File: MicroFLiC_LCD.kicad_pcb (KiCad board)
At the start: 2 copper layers, 50 x 50 mm, 21 parts, among them P1 CONN_02X08, Q1 BCX54-16, U1 MCP4728, U2 TLV2371, U3 74AHCT367, U4 74AHCT367

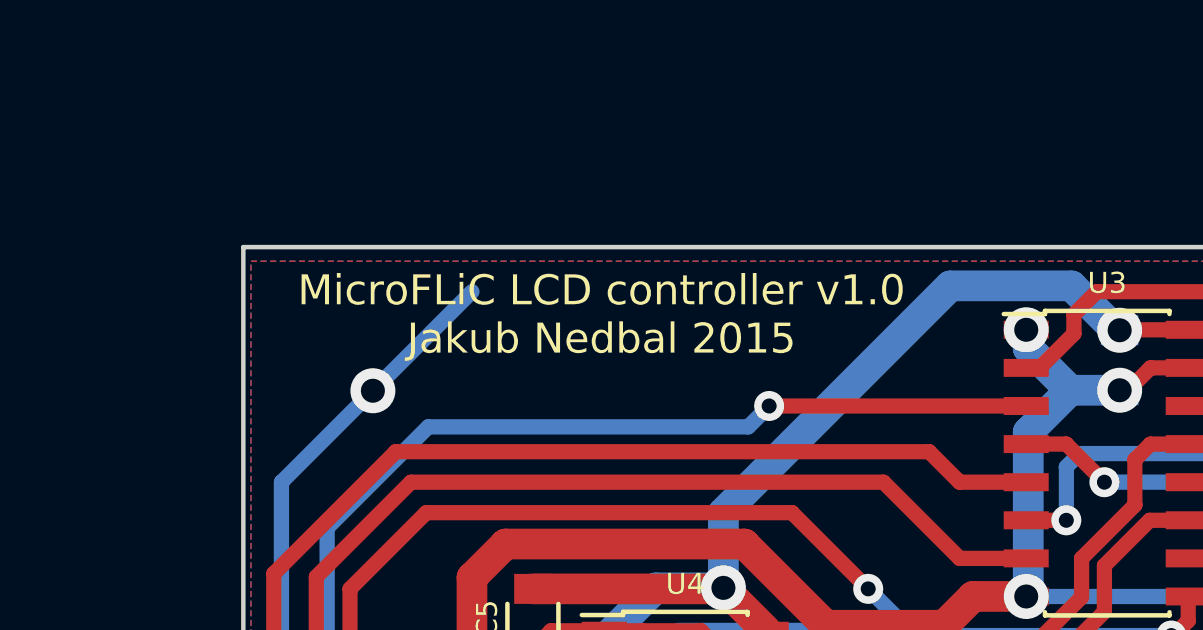
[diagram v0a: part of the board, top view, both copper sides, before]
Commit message: Renamed files, added part description
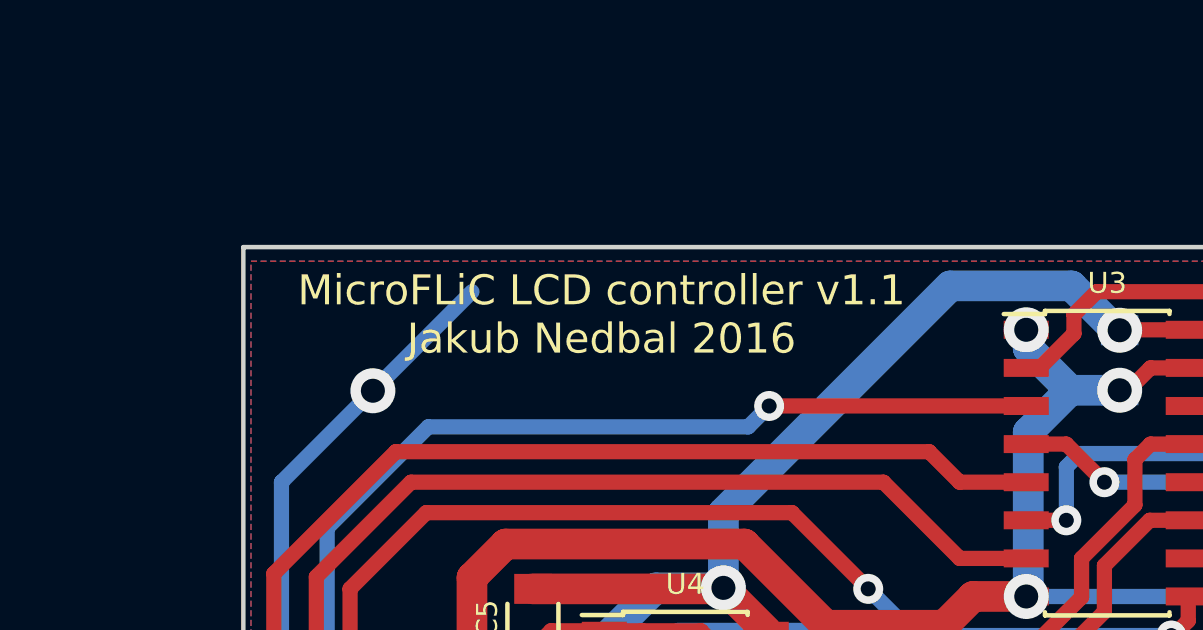
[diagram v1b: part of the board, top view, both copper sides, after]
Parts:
- A1: value Arduino Micro -> Arduino MICRO
- C1: value 10u -> 10u/10V
- C4, C5: value C -> 100n
- P1: value CONN_02X08 -> 2x8 header strip
- R2, R3: value 27R -> 18R(0.5W)
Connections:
- A1 pad 3.3V: (no net) -> Net-(A1-Pad3.3V)
- A1 pad AREF: (no net) -> Net-(A1-PadAREF)
- A1 pad RX: (no net) -> Net-(A1-PadRX)
- A1 pad TX: (no net) -> Net-(A1-PadTX)
- LCD1 pad 10: (no net) -> Net-(LCD1-Pad10)
- LCD1 pad 7: (no net) -> Net-(LCD1-Pad7)
- LCD1 pad 8: (no net) -> Net-(LCD1-Pad8)
- LCD1 pad 9: (no net) -> Net-(LCD1-Pad9)
- U1 pad 5: (no net) -> Net-(U1-Pad5)
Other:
- board text added: "MicroFLiC LCD controller v1.1 Jakub Nedbal 2016"
- board text removed: "MicroFLiC LCD controller v1.0 Jakub Nedbal 2015"
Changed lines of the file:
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@@
-(kicad_pcb (version 4) (host pcbnew 4.0.1-3.201512221402+6198~38~ubuntu14.04.1-stable)
+(kicad_pcb (version 4) (host pcbnew "(2015-12-10 BZR 6367)-product")
   (general
     (links 82)
     (no_connects 0)
-    (area 34.106999 100.104999 132.857001 160.855001)
+    (area 82.220999 110.198999 132.371001 160.349001)
     (thickness 1.6)
     (drawings 72)
@@
     (zones 0)
     (modules 21)
-    (nets 50)
+    (nets 59)
   )
   (page A4)
@@
       (drillshape 0)
       (scaleselection 1)
-      (outputdirectory board/))
+      (outputdirectory board_v1.1/))
   )
   (net 0 "")
@@
   (net 48 /3V3to5V/D4)
   (net 49 "Net-(R4-Pad2)")
+  (net 50 "Net-(A1-PadAREF)")
+  (net 51 "Net-(A1-Pad3.3V)")
+  (net 52 "Net-(A1-PadTX)")
+  (net 53 "Net-(A1-PadRX)")
+  (net 54 "Net-(LCD1-Pad7)")
+  (net 55 "Net-(LCD1-Pad8)")
+  (net 56 "Net-(LCD1-Pad9)")
+  (net 57 "Net-(LCD1-Pad10)")
+  (net 58 "Net-(U1-Pad5)")
   (net_class Default "This is the default net class."
     (clearance 0.2)
@@
     (add_net /~LDAC)
     (add_net GND)
+    (add_net "Net-(A1-Pad3.3V)")
+    (add_net "Net-(A1-PadAREF)")
     (add_net "Net-(A1-PadNC)")
+    (add_net "Net-(A1-PadRX)")
+    (add_net "Net-(A1-PadTX)")
+    (add_net "Net-(LCD1-Pad10)")
+    (add_net "Net-(LCD1-Pad7)")
+    (add_net "Net-(LCD1-Pad8)")
+    (add_net "Net-(LCD1-Pad9)")
     (add_net "Net-(Q1-Pad1)")
     (add_net "Net-(Q1-Pad3)")
@@
     (add_net "Net-(R2-Pad2)")
     (add_net "Net-(R4-Pad2)")
+    (add_net "Net-(U1-Pad5)")
   )
   (module jakub:ArduinoMicro (layer B.Cu)
@@
       (effects (font (size 1.2 1.2) (thickness 0.15)) (justify mirror))
     )
-    (fp_text value "Arduino Micro" (at 26.67 9.634) (layer B.SilkS)
+    (fp_text value "Arduino MICRO" (at 26.67 9.634) (layer B.SilkS)
       (effects (font (size 1.2 1.2) (thickness 0.15)) (justify mirror))
     )
@@
     (pad A0 thru_hole circle (at 36.52 16.62) (size 1.2 1.2) (drill 0.8) (layers *.Cu *.Mask B.SilkS)
       (net 9 /LCD_E))
-    (pad AREF thru_hole circle (at 39.06 16.62) (size 1.2 1.2) (drill 0.8) (layers *.Cu *.Mask B.SilkS))
-    (pad 3.3V thru_hole circle (at 41.6 16.62) (size 1.2 1.2) (drill 0.8) (layers *.Cu *.Mask B.SilkS))
+    (pad AREF thru_hole circle (at 39.06 16.62) (size 1.2 1.2) (drill 0.8) (layers *.Cu *.Mask B.SilkS)
+      (net 50 "Net-(A1-PadAREF)"))
+    (pad 3.3V thru_hole circle (at 41.6 16.62) (size 1.2 1.2) (drill 0.8) (layers *.Cu *.Mask B.SilkS)
+      (net 51 "Net-(A1-Pad3.3V)"))
     (pad 13 thru_hole circle (at 44.14 16.62) (size 1.2 1.2) (drill 0.8) (layers *.Cu *.Mask B.SilkS)
       (net 23 /D13))
@@
     (pad SS thru_hole circle (at 6.04 1.38) (size 1.2 1.2) (drill 0.8) (layers *.Cu *.Mask B.SilkS)
       (net 30 /3V3to5V/D0_5V))
-    (pad TX thru_hole circle (at 8.58 1.38) (size 1.2 1.2) (drill 0.8) (layers *.Cu *.Mask B.SilkS))
-    (pad RX thru_hole circle (at 11.12 1.38) (size 1.2 1.2) (drill 0.8) (layers *.Cu *.Mask B.SilkS))
+    (pad TX thru_hole circle (at 8.58 1.38) (size 1.2 1.2) (drill 0.8) (layers *.Cu *.Mask B.SilkS)
+      (net 52 "Net-(A1-PadTX)"))
+    (pad RX thru_hole circle (at 11.12 1.38) (size 1.2 1.2) (drill 0.8) (layers *.Cu *.Mask B.SilkS)
+      (net 53 "Net-(A1-PadRX)"))
     (pad RST thru_hole circle (at 13.66 1.38) (size 1.2 1.2) (drill 0.8) (layers *.Cu *.Mask B.SilkS)
       (net 25 /3V3to5V/~RST_5V))
@@
       (effects (font (size 0.7 0.7) (thickness 0.11)) (justify mirror))
     )
-    (fp_text value 10u (at 0 -2.1) (layer B.Fab) hide
+    (fp_text value 10u/10V (at 0 -2.1) (layer B.Fab) hide
       (effects (font (size 1 1) (thickness 0.15)) (justify mirror))
     )
@@
       (effects (font (size 0.7 0.7) (thickness 0.11)))
     )
-    (fp_text value 27R (at 0 2.1 180) (layer F.Fab) hide
+    (fp_text value "18R(0.5W)" (at 0 2.1 180) (layer F.Fab) hide
       (effects (font (size 1 1) (thickness 0.15)))
     )
@@
       (effects (font (size 0.7 0.7) (thickness 0.11)))
     )
-    (fp_text value 27R (at 0 2.1 90) (layer F.Fab) hide
+    (fp_text value "18R(0.5W)" (at 0 2.1 90) (layer F.Fab) hide
       (effects (font (size 1 1) (thickness 0.15)))
     )
@@
     (pad 4 smd rect (at -2.2 0.5) (size 1.4 0.3) (layers F.Cu F.Paste F.Mask)
       (net 13 /~LDAC))
-    (pad 5 smd rect (at -2.2 1) (size 1.4 0.3) (layers F.Cu F.Paste F.Mask))
+    (pad 5 smd rect (at -2.2 1) (size 1.4 0.3) (layers F.Cu F.Paste F.Mask)
+      (net 58 "Net-(U1-Pad5)"))
     (pad 6 smd rect (at 2.2 1) (size 1.4 0.3) (layers F.Cu F.Paste F.Mask)
       (net 22 /LCD_BKL_CTRL))
@@
       (effects (font (size 0.7 0.7) (thickness 0.11)) (justify mirror))
     )
-    (fp_text value CONN_02X08 (at 0 3.1 270) (layer B.Fab)
+    (fp_text value "2x8 header strip" (at 0 3.1 270) (layer B.Fab)
       (effects (font (size 1 1) (thickness 0.15)) (justify mirror))
     )
@@
       (effects (font (size 0.7 0.7) (thickness 0.11)) (justify mirror))
     )
-    (fp_text value C (at 0 -2.1 270) (layer B.Fab)
+    (fp_text value 100n (at 0 -2.1 270) (layer B.Fab)
       (effects (font (size 1 1) (thickness 0.15)) (justify mirror))
     )
@@
       (effects (font (size 0.7 0.7) (thickness 0.11)))
     )
-    (fp_text value C (at 0 2.1 360) (layer F.Fab) hide
+    (fp_text value 100n (at 0 2.1 360) (layer F.Fab) hide
       (effects (font (size 1 1) (thickness 0.15)))
     )
@@
     (pad 6 thru_hole circle (at 26.5 27) (size 1.9 1.9) (drill 1) (layers *.Cu *.Mask F.SilkS)
       (net 8 /LCD_D4))
-    (pad 7 thru_hole circle (at 23.96 27) (size 1.9 1.9) (drill 1) (layers *.Cu *.Mask F.SilkS))
-    (pad 8 thru_hole circle (at 21.42 27) (size 1.9 1.9) (drill 1) (layers *.Cu *.Mask F.SilkS))
-    (pad 9 thru_hole circle (at 18.88 27) (size 1.9 1.9) (drill 1) (layers *.Cu *.Mask F.SilkS))
-    (pad 10 thru_hole circle (at 16.34 27) (size 1.9 1.9) (drill 1) (layers *.Cu *.Mask F.SilkS))
+    (pad 7 thru_hole circle (at 23.96 27) (size 1.9 1.9) (drill 1) (layers *.Cu *.Mask F.SilkS)
+      (net 54 "Net-(LCD1-Pad7)"))
+    (pad 8 thru_hole circle (at 21.42 27) (size 1.9 1.9) (drill 1) (layers *.Cu *.Mask F.SilkS)
+      (net 55 "Net-(LCD1-Pad8)"))
+    (pad 9 thru_hole circle (at 18.88 27) (size 1.9 1.9) (drill 1) (layers *.Cu *.Mask F.SilkS)
+      (net 56 "Net-(LCD1-Pad9)"))
+    (pad 10 thru_hole circle (at 16.34 27) (size 1.9 1.9) (drill 1) (layers *.Cu *.Mask F.SilkS)
+      (net 57 "Net-(LCD1-Pad10)"))
     (pad 11 thru_hole circle (at 13.8 27) (size 1.9 1.9) (drill 1) (layers *.Cu *.Mask F.SilkS)
       (net 9 /LCD_E))
@@
     (effects (font (size 1 1) (thickness 0.12)))
   )
-  (gr_text "MicroFLiC LCD controller v1.0\nJakub Nedbal 2015" (at 94.234 112.522) (layer B.SilkS)
+  (gr_text "MicroFLiC LCD controller v1.1\nJakub Nedbal 2016" (at 94.234 112.522) (layer B.SilkS)
     (effects (font (size 1 1) (thickness 0.12)) (justify mirror))
   )
-  (gr_text "MicroFLiC LCD controller v1.0\nJakub Nedbal 2015" (at 94.234 112.522) (layer F.SilkS)
+  (gr_text "MicroFLiC LCD controller v1.1\nJakub Nedbal 2016" (at 94.234 112.522) (layer F.SilkS)
     (effects (font (size 1 1) (thickness 0.12)))
   )

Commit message: Fixed label of 1k5 resistor
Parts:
- R4: value 1K5 -> 1k5
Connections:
- A1 pad 3.3V: Net-(A1-Pad3.3V) -> (no net)
- A1 pad AREF: Net-(A1-PadAREF) -> (no net)
- A1 pad RX: Net-(A1-PadRX) -> (no net)
- A1 pad TX: Net-(A1-PadTX) -> (no net)
- LCD1 pad 10: Net-(LCD1-Pad10) -> (no net)
- LCD1 pad 7: Net-(LCD1-Pad7) -> (no net)
- LCD1 pad 8: Net-(LCD1-Pad8) -> (no net)
- LCD1 pad 9: Net-(LCD1-Pad9) -> (no net)
- U1 pad 5: Net-(U1-Pad5) -> (no net)
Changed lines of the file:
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@@
-(kicad_pcb (version 4) (host pcbnew "(2015-12-10 BZR 6367)-product")
+(kicad_pcb (version 4) (host pcbnew 4.0.2-4+6225~38~ubuntu14.04.1-stable)
   (general
     (links 82)
@@
     (zones 0)
     (modules 21)
-    (nets 59)
+    (nets 50)
   )
   (page A4)
@@
   (net 48 /3V3to5V/D4)
   (net 49 "Net-(R4-Pad2)")
-  (net 50 "Net-(A1-PadAREF)")
-  (net 51 "Net-(A1-Pad3.3V)")
-  (net 52 "Net-(A1-PadTX)")
-  (net 53 "Net-(A1-PadRX)")
-  (net 54 "Net-(LCD1-Pad7)")
-  (net 55 "Net-(LCD1-Pad8)")
-  (net 56 "Net-(LCD1-Pad9)")
-  (net 57 "Net-(LCD1-Pad10)")
-  (net 58 "Net-(U1-Pad5)")
   (net_class Default "This is the default net class."
     (clearance 0.2)
@@
     (add_net /~LDAC)
     (add_net GND)
-    (add_net "Net-(A1-Pad3.3V)")
-    (add_net "Net-(A1-PadAREF)")
     (add_net "Net-(A1-PadNC)")
-    (add_net "Net-(A1-PadRX)")
-    (add_net "Net-(A1-PadTX)")
-    (add_net "Net-(LCD1-Pad10)")
-    (add_net "Net-(LCD1-Pad7)")
-    (add_net "Net-(LCD1-Pad8)")
-    (add_net "Net-(LCD1-Pad9)")
     (add_net "Net-(Q1-Pad1)")
     (add_net "Net-(Q1-Pad3)")
@@
     (add_net "Net-(R2-Pad2)")
     (add_net "Net-(R4-Pad2)")
-    (add_net "Net-(U1-Pad5)")
   )
   (module jakub:ArduinoMicro (layer B.Cu)
@@
     (pad A0 thru_hole circle (at 36.52 16.62) (size 1.2 1.2) (drill 0.8) (layers *.Cu *.Mask B.SilkS)
       (net 9 /LCD_E))
-    (pad AREF thru_hole circle (at 39.06 16.62) (size 1.2 1.2) (drill 0.8) (layers *.Cu *.Mask B.SilkS)
-      (net 50 "Net-(A1-PadAREF)"))
-    (pad 3.3V thru_hole circle (at 41.6 16.62) (size 1.2 1.2) (drill 0.8) (layers *.Cu *.Mask B.SilkS)
-      (net 51 "Net-(A1-Pad3.3V)"))
+    (pad AREF thru_hole circle (at 39.06 16.62) (size 1.2 1.2) (drill 0.8) (layers *.Cu *.Mask B.SilkS))
+    (pad 3.3V thru_hole circle (at 41.6 16.62) (size 1.2 1.2) (drill 0.8) (layers *.Cu *.Mask B.SilkS))
     (pad 13 thru_hole circle (at 44.14 16.62) (size 1.2 1.2) (drill 0.8) (layers *.Cu *.Mask B.SilkS)
       (net 23 /D13))
@@
     (pad SS thru_hole circle (at 6.04 1.38) (size 1.2 1.2) (drill 0.8) (layers *.Cu *.Mask B.SilkS)
       (net 30 /3V3to5V/D0_5V))
-    (pad TX thru_hole circle (at 8.58 1.38) (size 1.2 1.2) (drill 0.8) (layers *.Cu *.Mask B.SilkS)
-      (net 52 "Net-(A1-PadTX)"))
-    (pad RX thru_hole circle (at 11.12 1.38) (size 1.2 1.2) (drill 0.8) (layers *.Cu *.Mask B.SilkS)
-      (net 53 "Net-(A1-PadRX)"))
+    (pad TX thru_hole circle (at 8.58 1.38) (size 1.2 1.2) (drill 0.8) (layers *.Cu *.Mask B.SilkS))
+    (pad RX thru_hole circle (at 11.12 1.38) (size 1.2 1.2) (drill 0.8) (layers *.Cu *.Mask B.SilkS))
     (pad RST thru_hole circle (at 13.66 1.38) (size 1.2 1.2) (drill 0.8) (layers *.Cu *.Mask B.SilkS)
       (net 25 /3V3to5V/~RST_5V))
@@
     (pad 4 smd rect (at -2.2 0.5) (size 1.4 0.3) (layers F.Cu F.Paste F.Mask)
       (net 13 /~LDAC))
-    (pad 5 smd rect (at -2.2 1) (size 1.4 0.3) (layers F.Cu F.Paste F.Mask)
-      (net 58 "Net-(U1-Pad5)"))
+    (pad 5 smd rect (at -2.2 1) (size 1.4 0.3) (layers F.Cu F.Paste F.Mask))
     (pad 6 smd rect (at 2.2 1) (size 1.4 0.3) (layers F.Cu F.Paste F.Mask)
       (net 22 /LCD_BKL_CTRL))
@@
       (effects (font (size 0.7 0.7) (thickness 0.11)) (justify mirror))
     )
-    (fp_text value 1K5 (at 0 -2.1 90) (layer B.Fab)
+    (fp_text value 1k5 (at 0 -2.1 90) (layer B.Fab)
       (effects (font (size 1 1) (thickness 0.15)) (justify mirror))
     )
@@
     (pad 6 thru_hole circle (at 26.5 27) (size 1.9 1.9) (drill 1) (layers *.Cu *.Mask F.SilkS)
       (net 8 /LCD_D4))
-    (pad 7 thru_hole circle (at 23.96 27) (size 1.9 1.9) (drill 1) (layers *.Cu *.Mask F.SilkS)
-      (net 54 "Net-(LCD1-Pad7)"))
-    (pad 8 thru_hole circle (at 21.42 27) (size 1.9 1.9) (drill 1) (layers *.Cu *.Mask F.SilkS)
-      (net 55 "Net-(LCD1-Pad8)"))
-    (pad 9 thru_hole circle (at 18.88 27) (size 1.9 1.9) (drill 1) (layers *.Cu *.Mask F.SilkS)
-      (net 56 "Net-(LCD1-Pad9)"))
-    (pad 10 thru_hole circle (at 16.34 27) (size 1.9 1.9) (drill 1) (layers *.Cu *.Mask F.SilkS)
-      (net 57 "Net-(LCD1-Pad10)"))
+    (pad 7 thru_hole circle (at 23.96 27) (size 1.9 1.9) (drill 1) (layers *.Cu *.Mask F.SilkS))
+    (pad 8 thru_hole circle (at 21.42 27) (size 1.9 1.9) (drill 1) (layers *.Cu *.Mask F.SilkS))
+    (pad 9 thru_hole circle (at 18.88 27) (size 1.9 1.9) (drill 1) (layers *.Cu *.Mask F.SilkS))
+    (pad 10 thru_hole circle (at 16.34 27) (size 1.9 1.9) (drill 1) (layers *.Cu *.Mask F.SilkS))
     (pad 11 thru_hole circle (at 13.8 27) (size 1.9 1.9) (drill 1) (layers *.Cu *.Mask F.SilkS)
       (net 9 /LCD_E))
